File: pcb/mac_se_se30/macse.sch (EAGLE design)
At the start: 8 parts, among them J1 ATX24RH

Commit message: mac SE adaptor done
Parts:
- JP1: device pinhead:PINHD-1X3 -> atx_power_control:PINHD-1X4
- JP4: device atx_power_control:PINHD-1X4 -> adafruit_changed:PINHD-1X6
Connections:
- removed net N$7: JP1.2, JP4.3
- net +12V: now also JP1.3; no longer JP1.1
- net +5V: now also JP4.3; no longer JP1.3
- net GND: now also JP1.4
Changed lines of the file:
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@@
 </classes>
 <parts>
-<part name="GND1" library="supply1" library_urn="urn:adsk.eagle:library:371" deviceset="GND" device=""/>
 <part name="J1" library="atx4vc" deviceset="ATX24" device="RH"/>
 <part name="GND2" library="supply1" library_urn="urn:adsk.eagle:library:371" deviceset="GND" device=""/>
@@
 <part name="P-1" library="supply1" library_urn="urn:adsk.eagle:library:371" deviceset="-12V" device=""/>
 <part name="J7" library="atx_power_control" deviceset="CONN_02" device="3.5MM-NO_SILK"/>
-<part name="JP4" library="atx_power_control" deviceset="PINHD-1X4" device=""/>
+<part name="JP4" library="adafruit_changed" deviceset="PINHD-1X6" device=""/>
 <part name="U$8" library="atx_power_control" deviceset="CAR_FUSE_HOLDER" device="3IN1"/>
 <part name="U$2" library="atx_power_control" deviceset="CAR_FUSE_HOLDER" device="3IN1"/>
-<part name="JP1" library="pinhead" library_urn="urn:adsk.eagle:library:325" deviceset="PINHD-1X3" device="" package3d_urn="urn:adsk.eagle:package:22458/2"/>
 <part name="JP2" library="pinhead" library_urn="urn:adsk.eagle:library:325" deviceset="PINHD-1X2" device="" package3d_urn="urn:adsk.eagle:package:22435/2"/>
 <part name="P+3" library="supply1" library_urn="urn:adsk.eagle:library:371" deviceset="+5V" device=""/>
 <part name="P+1" library="supply1" library_urn="urn:adsk.eagle:library:371" deviceset="+12V" device=""/>
 <part name="P-2" library="supply1" library_urn="urn:adsk.eagle:library:371" deviceset="-12V" device=""/>
-<part name="P+4" library="supply1" library_urn="urn:adsk.eagle:library:371" deviceset="+5V" device=""/>
 <part name="GND3" library="supply1" library_urn="urn:adsk.eagle:library:371" deviceset="GND" device=""/>
 <part name="GND4" library="supply1" library_urn="urn:adsk.eagle:library:371" deviceset="GND" device=""/>
 <part name="P+5" library="supply1" library_urn="urn:adsk.eagle:library:371" deviceset="+12V" device=""/>
-<part name="P+6" library="supply1" library_urn="urn:adsk.eagle:library:371" deviceset="+5V" device=""/>
-<part name="GND5" library="supply1" library_urn="urn:adsk.eagle:library:371" deviceset="GND" device=""/>
 <part name="U$1" library="atx4vc" deviceset="MACSE" device=""/>
 <part name="GND6" library="supply1" library_urn="urn:adsk.eagle:library:371" deviceset="GND" device=""/>
 <part name="P+7" library="supply1" library_urn="urn:adsk.eagle:library:371" deviceset="+5V" device=""/>
+<part name="JP1" library="atx_power_control" deviceset="PINHD-1X4" device=""/>
+<part name="GND7" library="supply1" library_urn="urn:adsk.eagle:library:371" deviceset="GND" device=""/>
+<part name="P+9" library="supply1" library_urn="urn:adsk.eagle:library:371" deviceset="+5V" device=""/>
 </parts>
 <sheets>
@@
 </plain>
 <instances>
-<instance part="GND1" gate="1" x="157.48" y="88.9" smashed="yes">
-<attribute name="VALUE" x="154.94" y="86.36" size="1.778" layer="96"/>
-</instance>
 <instance part="J1" gate="G$1" x="96.52" y="175.26" smashed="yes">
 <attribute name="NAME" x="83.82" y="195.58" size="1.27" layer="95"/>
@@
 <attribute name="NAME" x="167.64" y="156.972" size="1.778" layer="95" font="vector" rot="R180"/>
 </instance>
-<instance part="JP4" gate="A" x="-15.24" y="101.6" smashed="yes">
-<attribute name="NAME" x="-21.59" y="109.855" size="1.778" layer="95"/>
-<attribute name="VALUE" x="-21.59" y="93.98" size="1.778" layer="96"/>
+<instance part="JP4" gate="A" x="-15.24" y="99.06" smashed="yes">
+<attribute name="NAME" x="-21.59" y="107.315" size="1.778" layer="95"/>
+<attribute name="VALUE" x="-21.59" y="91.44" size="1.778" layer="96"/>
 </instance>
 <instance part="U$8" gate="G$1" x="38.1" y="187.96" smashed="yes"/>
 <instance part="U$2" gate="G$1" x="154.94" y="175.26" smashed="yes"/>
-<instance part="JP1" gate="A" x="5.08" y="101.6" smashed="yes">
-<attribute name="NAME" x="-1.27" y="107.315" size="1.778" layer="95"/>
-<attribute name="VALUE" x="-1.27" y="93.98" size="1.778" layer="96"/>
-</instance>
 <instance part="JP2" gate="G$1" x="180.34" y="160.02" smashed="yes">
 <attribute name="NAME" x="173.99" y="165.735" size="1.778" layer="95"/>
@@
 <attribute name="VALUE" x="114.3" y="101.6" size="1.778" layer="96" rot="MR90"/>
 </instance>
-<instance part="P+4" gate="1" x="149.86" y="109.22" smashed="yes">
-<attribute name="VALUE" x="147.32" y="104.14" size="1.778" layer="96" rot="R90"/>
-</instance>
 <instance part="GND3" gate="1" x="149.86" y="157.48" smashed="yes">
 <attribute name="VALUE" x="147.32" y="154.94" size="1.778" layer="96"/>
@@
 <attribute name="VALUE" x="-30.48" y="93.98" size="1.778" layer="96"/>
 </instance>
-<instance part="P+5" gate="1" x="15.24" y="106.68" smashed="yes" rot="MR0">
-<attribute name="VALUE" x="17.78" y="101.6" size="1.778" layer="96" rot="MR90"/>
-</instance>
-<instance part="P+6" gate="1" x="25.4" y="101.6" smashed="yes">
-<attribute name="VALUE" x="22.86" y="96.52" size="1.778" layer="96" rot="R90"/>
-</instance>
-<instance part="GND5" gate="1" x="177.8" y="73.66" smashed="yes">
-<attribute name="VALUE" x="175.26" y="71.12" size="1.778" layer="96"/>
+<instance part="P+5" gate="1" x="-7.62" y="137.16" smashed="yes" rot="MR0">
+<attribute name="VALUE" x="-5.08" y="132.08" size="1.778" layer="96" rot="MR90"/>
 </instance>
 <instance part="U$1" gate="G$1" x="83.82" y="109.22" smashed="yes"/>
@@
 <instance part="P+7" gate="1" x="121.92" y="119.38" smashed="yes">
 <attribute name="VALUE" x="119.38" y="114.3" size="1.778" layer="96" rot="R90"/>
+</instance>
+<instance part="JP1" gate="A" x="-15.24" y="134.62" smashed="yes">
+<attribute name="NAME" x="-21.59" y="142.875" size="1.778" layer="95"/>
+<attribute name="VALUE" x="-21.59" y="127" size="1.778" layer="96"/>
+</instance>
+<instance part="GND7" gate="1" x="-27.94" y="129.54" smashed="yes">
+<attribute name="VALUE" x="-30.48" y="127" size="1.778" layer="96"/>
+</instance>
+<instance part="P+9" gate="1" x="-5.08" y="104.14" smashed="yes">
+<attribute name="VALUE" x="-7.62" y="99.06" size="1.778" layer="96" rot="R90"/>
 </instance>
 </instances>
@@
 <junction x="106.68" y="96.52"/>
 </segment>
+<segment>
+<pinref part="JP1" gate="A" pin="4"/>
+<pinref part="GND7" gate="1" pin="GND"/>
+<wire x1="-17.78" y1="132.08" x2="-27.94" y2="132.08" width="0.1524" layer="91"/>
+</segment>
 </net>
 <net name="-12V" class="0">
@@
 </segment>
 <segment>
-<pinref part="JP1" gate="A" pin="3"/>
-<pinref part="P+6" gate="1" pin="+5V"/>
-<wire x1="2.54" y1="99.06" x2="25.4" y2="99.06" width="0.1524" layer="91"/>
-</segment>
-<segment>
 <pinref part="U$1" gate="G$1" pin="P$4"/>
 <pinref part="P+7" gate="1" pin="+5V"/>
@@
 <wire x1="121.92" y1="91.44" x2="73.66" y2="91.44" width="0.1524" layer="91"/>
 <junction x="121.92" y="116.84"/>
+</segment>
+<segment>
+<pinref part="JP4" gate="A" pin="3"/>
+<pinref part="P+9" gate="1" pin="+5V"/>
+<wire x1="-17.78" y1="101.6" x2="-5.08" y2="101.6" width="0.1524" layer="91"/>
 </segment>
 </net>
@@
 </segment>
 <segment>
-<pinref part="P+5" gate="1" pin="+12V"/>
-<pinref part="JP1" gate="A" pin="1"/>
-<wire x1="15.24" y1="104.14" x2="2.54" y2="104.14" width="0.1524" layer="91"/>
-</segment>
-<segment>
 <pinref part="U$1" gate="G$1" pin="P$5"/>
 <pinref part="P+1" gate="1" pin="+12V"/>
@@
 <junction x="53.34" y="111.76"/>
 </segment>
+<segment>
+<pinref part="JP1" gate="A" pin="3"/>
+<pinref part="P+5" gate="1" pin="+12V"/>
+<wire x1="-17.78" y1="134.62" x2="-7.62" y2="134.62" width="0.1524" layer="91"/>
+</segment>
 </net>
 <net name="N$5" class="0">
@@
 </segment>
 </net>
-<net name="N$7" class="0">
-<segment>
-<pinref part="JP1" gate="A" pin="2"/>
-<pinref part="JP4" gate="A" pin="3"/>
-<wire x1="2.54" y1="101.6" x2="-17.78" y2="101.6" width="0.1524" layer="91"/>
-</segment>
-</net>

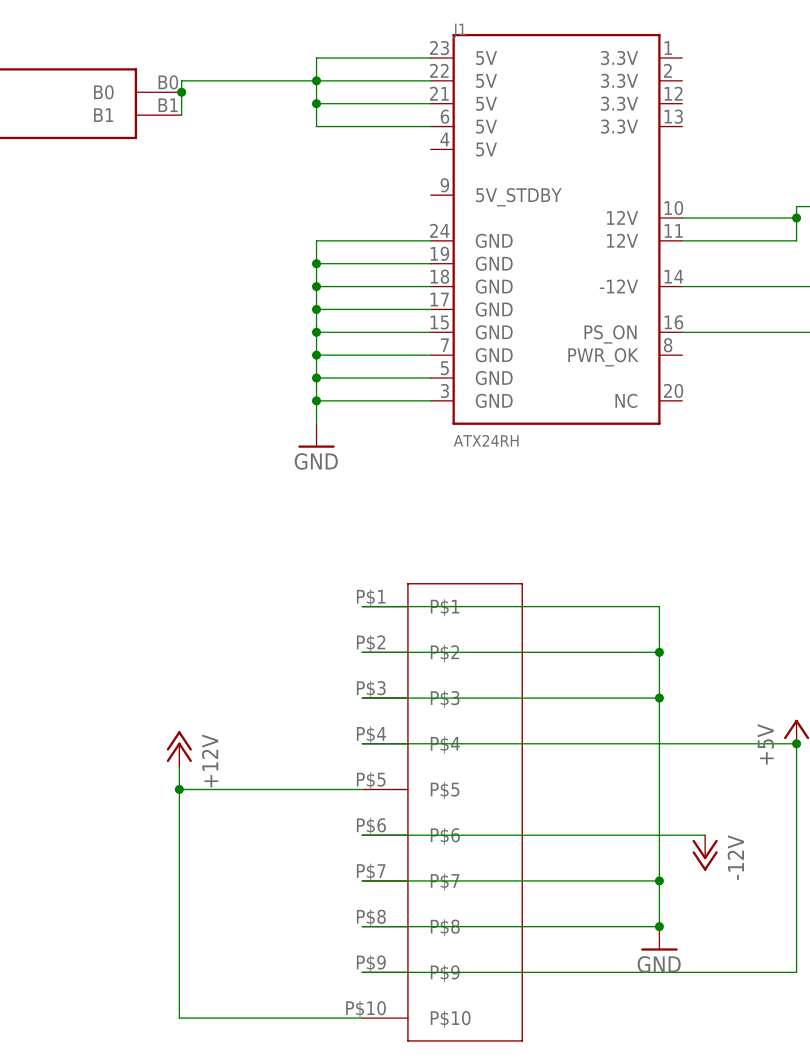
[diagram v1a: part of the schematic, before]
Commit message: updating mac SE atx adaptor
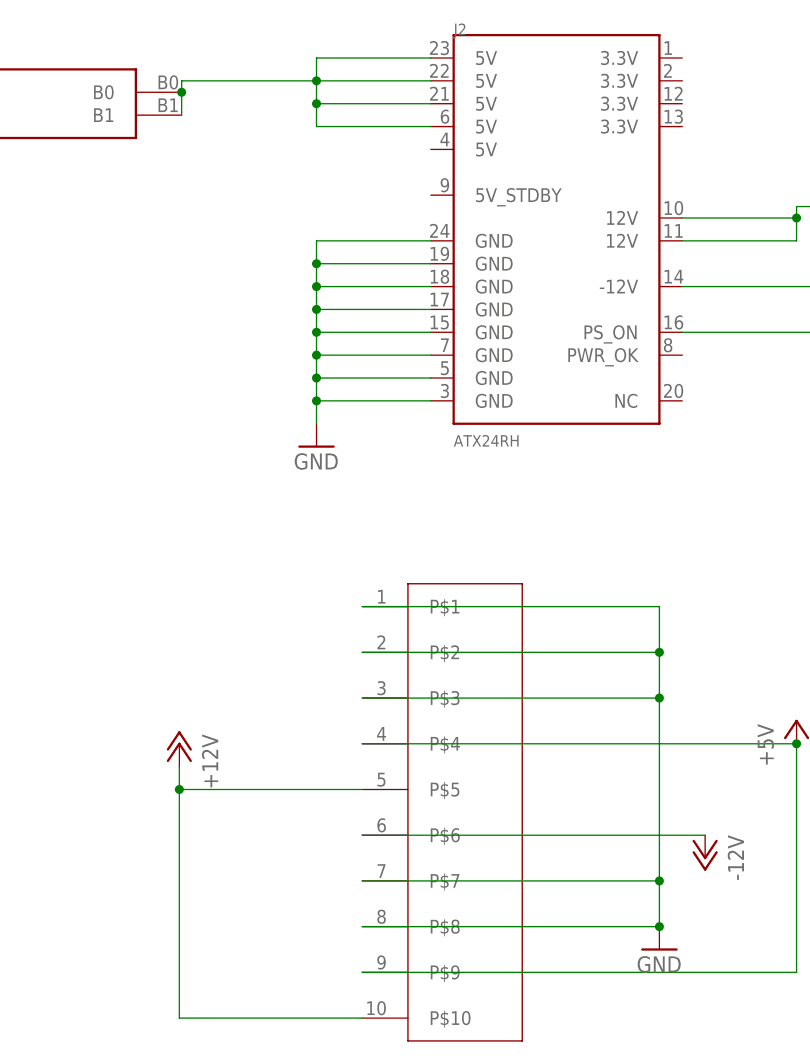
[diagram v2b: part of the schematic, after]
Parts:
- removed J1: ATX24RH, atx4vc:ATX24RH
- added J2: ATX24RH, SparkFun-Connectors:ATX24RH
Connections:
- net -12V: now also J2.-12V; no longer J1.-12V
- net GND: now also J2.GND@0, J2.GND@1, J2.GND@2, J2.GND@3, J2.GND@4, J2.GND@5, J2.GND@6, J2.GND@7; no longer J1.GND@0, J1.GND@1, J1.GND@2, J1.GND@3, J1.GND@4, J1.GND@5, J1.GND@6, J1.GND@7
- net N$5: now also J2.PS_ON; no longer J1.PS_ON
- net N$6: now also J2.5V@1, J2.5V@2, J2.5V@3, J2.5V@4; no longer J1.5V@1, J1.5V@2, J1.5V@3, J1.5V@4
- net N$8: now also J2.12V@0, J2.12V@1; no longer J1.12V@0, J1.12V@1
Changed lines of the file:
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@@
 </classes>
 <parts>
-<part name="J1" library="atx4vc" deviceset="ATX24" device="RH"/>
 <part name="GND2" library="supply1" library_urn="urn:adsk.eagle:library:371" deviceset="GND" device=""/>
 <part name="P+2" library="supply1" library_urn="urn:adsk.eagle:library:371" deviceset="+12V" device=""/>
@@
 <part name="GND7" library="supply1" library_urn="urn:adsk.eagle:library:371" deviceset="GND" device=""/>
 <part name="P+9" library="supply1" library_urn="urn:adsk.eagle:library:371" deviceset="+5V" device=""/>
+<part name="J2" library="SparkFun-Connectors" deviceset="ATX24" device="RH"/>
 </parts>
 <sheets>
@@
 </plain>
 <instances>
-<instance part="J1" gate="G$1" x="96.52" y="175.26" smashed="yes">
-<attribute name="NAME" x="83.82" y="195.58" size="1.27" layer="95"/>
-<attribute name="VALUE" x="83.82" y="149.86" size="1.27" layer="96"/>
-</instance>
 <instance part="GND2" gate="1" x="68.58" y="149.86" smashed="yes">
 <attribute name="VALUE" x="66.04" y="147.32" size="1.778" layer="96"/>
@@
 <attribute name="VALUE" x="-7.62" y="99.06" size="1.778" layer="96" rot="R90"/>
 </instance>
+<instance part="J2" gate="G$1" x="96.52" y="175.26" smashed="yes">
+<attribute name="NAME" x="83.82" y="195.58" size="1.27" layer="95"/>
+<attribute name="VALUE" x="83.82" y="149.86" size="1.27" layer="96"/>
+</instance>
 </instances>
 <busses>
@@
 <net name="GND" class="0">
 <segment>
-<pinref part="J1" gate="G$1" pin="GND@7"/>
 <pinref part="GND2" gate="1" pin="GND"/>
 <wire x1="81.28" y1="172.72" x2="68.58" y2="172.72" width="0.1524" layer="91"/>
 <wire x1="68.58" y1="172.72" x2="68.58" y2="170.18" width="0.1524" layer="91"/>
-<pinref part="J1" gate="G$1" pin="GND@6"/>
 <wire x1="68.58" y1="170.18" x2="68.58" y2="167.64" width="0.1524" layer="91"/>
 <wire x1="68.58" y1="167.64" x2="68.58" y2="165.1" width="0.1524" layer="91"/>
@@
 <wire x1="81.28" y1="170.18" x2="68.58" y2="170.18" width="0.1524" layer="91"/>
 <junction x="68.58" y="170.18"/>
-<pinref part="J1" gate="G$1" pin="GND@5"/>
 <wire x1="68.58" y1="167.64" x2="81.28" y2="167.64" width="0.1524" layer="91"/>
 <junction x="68.58" y="167.64"/>
-<pinref part="J1" gate="G$1" pin="GND@4"/>
 <wire x1="81.28" y1="165.1" x2="68.58" y2="165.1" width="0.1524" layer="91"/>
 <junction x="68.58" y="165.1"/>
-<pinref part="J1" gate="G$1" pin="GND@3"/>
 <wire x1="68.58" y1="162.56" x2="81.28" y2="162.56" width="0.1524" layer="91"/>
 <junction x="68.58" y="162.56"/>
-<pinref part="J1" gate="G$1" pin="GND@2"/>
 <wire x1="81.28" y1="160.02" x2="68.58" y2="160.02" width="0.1524" layer="91"/>
 <junction x="68.58" y="160.02"/>
-<pinref part="J1" gate="G$1" pin="GND@1"/>
 <wire x1="68.58" y1="157.48" x2="81.28" y2="157.48" width="0.1524" layer="91"/>
 <junction x="68.58" y="157.48"/>
-<pinref part="J1" gate="G$1" pin="GND@0"/>
 <wire x1="81.28" y1="154.94" x2="68.58" y2="154.94" width="0.1524" layer="91"/>
 <junction x="68.58" y="154.94"/>
+<pinref part="J2" gate="G$1" pin="GND@0"/>
+<pinref part="J2" gate="G$1" pin="GND@1"/>
+<pinref part="J2" gate="G$1" pin="GND@2"/>
+<pinref part="J2" gate="G$1" pin="GND@3"/>
+<pinref part="J2" gate="G$1" pin="GND@4"/>
+<pinref part="J2" gate="G$1" pin="GND@5"/>
+<pinref part="J2" gate="G$1" pin="GND@6"/>
+<pinref part="J2" gate="G$1" pin="GND@7"/>
 </segment>
 <segment>
@@
 <segment>
 <pinref part="P-1" gate="1" pin="-12V"/>
-<pinref part="J1" gate="G$1" pin="-12V"/>
 <wire x1="137.16" y1="167.64" x2="109.22" y2="167.64" width="0.1524" layer="91"/>
+<pinref part="J2" gate="G$1" pin="-12V"/>
 </segment>
 <segment>
@@
 <net name="N$6" class="0">
 <segment>
-<pinref part="J1" gate="G$1" pin="5V@4"/>
 <wire x1="81.28" y1="193.04" x2="68.58" y2="193.04" width="0.1524" layer="91"/>
-<pinref part="J1" gate="G$1" pin="5V@3"/>
 <wire x1="81.28" y1="190.5" x2="68.58" y2="190.5" width="0.1524" layer="91"/>
 <wire x1="68.58" y1="190.5" x2="68.58" y2="193.04" width="0.1524" layer="91"/>
-<pinref part="J1" gate="G$1" pin="5V@2"/>
 <wire x1="81.28" y1="187.96" x2="68.58" y2="187.96" width="0.1524" layer="91"/>
 <wire x1="68.58" y1="187.96" x2="68.58" y2="190.5" width="0.1524" layer="91"/>
 <junction x="68.58" y="190.5"/>
-<pinref part="J1" gate="G$1" pin="5V@1"/>
 <wire x1="81.28" y1="185.42" x2="68.58" y2="185.42" width="0.1524" layer="91"/>
 <wire x1="68.58" y1="185.42" x2="68.58" y2="187.96" width="0.1524" layer="91"/>
@@
 <wire x1="53.594" y1="190.5" x2="53.594" y2="189.23" width="0.1524" layer="91"/>
 <junction x="53.594" y="189.23"/>
+<pinref part="J2" gate="G$1" pin="5V@1"/>
+<pinref part="J2" gate="G$1" pin="5V@2"/>
+<pinref part="J2" gate="G$1" pin="5V@3"/>
+<pinref part="J2" gate="G$1" pin="5V@4"/>
 </segment>
 </net>
@@
 <net name="N$8" class="0">
 <segment>
-<pinref part="J1" gate="G$1" pin="12V@1"/>
 <wire x1="109.22" y1="172.72" x2="121.92" y2="172.72" width="0.1524" layer="91"/>
-<pinref part="J1" gate="G$1" pin="12V@0"/>
 <wire x1="109.22" y1="175.26" x2="121.92" y2="175.26" width="0.1524" layer="91"/>
 <wire x1="121.92" y1="175.26" x2="121.92" y2="172.72" width="0.1524" layer="91"/>
@@
 <wire x1="139.954" y1="173.99" x2="139.954" y2="176.53" width="0.1524" layer="91"/>
 <junction x="139.954" y="176.53"/>
+<pinref part="J2" gate="G$1" pin="12V@0"/>
+<pinref part="J2" gate="G$1" pin="12V@1"/>
 </segment>
 </net>
@@
 <net name="N$5" class="0">
 <segment>
-<pinref part="J1" gate="G$1" pin="PS_ON"/>
 <wire x1="109.22" y1="162.56" x2="157.48" y2="162.56" width="0.1524" layer="91"/>
 <pinref part="J7" gate="G$1" pin="1"/>
@@
 <wire x1="177.8" y1="162.56" x2="157.48" y2="162.56" width="0.1524" layer="91"/>
 <junction x="157.48" y="162.56"/>
-</segment>
-</net>
+<pinref part="J2" gate="G$1" pin="PS_ON"/>
+</segment>
+</net>

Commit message: updated mac SE pcb
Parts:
- removed JP4: (no value), adafruit_changed:PINHD-1X6
- added JP3: (no value), atx_power_control:PINHD-1X4
- added TP1: PTR1PAD1-20Y, testpad:PTR1PAD1-20Y
- J2: device SparkFun-Connectors:ATX24RH -> macse:ATX24RH
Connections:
- net +5V: now also JP3.3; no longer JP4.3
- net GND: now also JP3.4, TP1.TP; no longer JP4.4
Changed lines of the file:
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@@
 <part name="P-1" library="supply1" library_urn="urn:adsk.eagle:library:371" deviceset="-12V" device=""/>
 <part name="J7" library="atx_power_control" deviceset="CONN_02" device="3.5MM-NO_SILK"/>
-<part name="JP4" library="adafruit_changed" deviceset="PINHD-1X6" device=""/>
 <part name="U$8" library="atx_power_control" deviceset="CAR_FUSE_HOLDER" device="3IN1"/>
 <part name="U$2" library="atx_power_control" deviceset="CAR_FUSE_HOLDER" device="3IN1"/>
@@
 <part name="GND7" library="supply1" library_urn="urn:adsk.eagle:library:371" deviceset="GND" device=""/>
 <part name="P+9" library="supply1" library_urn="urn:adsk.eagle:library:371" deviceset="+5V" device=""/>
-<part name="J2" library="SparkFun-Connectors" deviceset="ATX24" device="RH"/>
+<part name="J2" library="macse" deviceset="ATX24" device="RH"/>
+<part name="JP3" library="atx_power_control" deviceset="PINHD-1X4" device=""/>
+<part name="TP1" library="testpad" library_urn="urn:adsk.eagle:library:385" deviceset="PTR1" device="PAD1-20Y" package3d_urn="urn:adsk.eagle:package:27951/1"/>
+<part name="GND1" library="supply1" library_urn="urn:adsk.eagle:library:371" deviceset="GND" device=""/>
 </parts>
 <sheets>
@@
 <attribute name="NAME" x="167.64" y="156.972" size="1.778" layer="95" font="vector" rot="R180"/>
 </instance>
-<instance part="JP4" gate="A" x="-15.24" y="99.06" smashed="yes">
-<attribute name="NAME" x="-21.59" y="107.315" size="1.778" layer="95"/>
-<attribute name="VALUE" x="-21.59" y="91.44" size="1.778" layer="96"/>
-</instance>
 <instance part="U$8" gate="G$1" x="38.1" y="187.96" smashed="yes"/>
 <instance part="U$2" gate="G$1" x="154.94" y="175.26" smashed="yes"/>
@@
 <attribute name="VALUE" x="147.32" y="154.94" size="1.778" layer="96"/>
 </instance>
-<instance part="GND4" gate="1" x="-27.94" y="96.52" smashed="yes">
-<attribute name="VALUE" x="-30.48" y="93.98" size="1.778" layer="96"/>
+<instance part="GND4" gate="1" x="-27.94" y="93.98" smashed="yes">
+<attribute name="VALUE" x="-30.48" y="91.44" size="1.778" layer="96"/>
 </instance>
 <instance part="P+5" gate="1" x="-7.62" y="137.16" smashed="yes" rot="MR0">
@@
 <attribute name="VALUE" x="-30.48" y="127" size="1.778" layer="96"/>
 </instance>
-<instance part="P+9" gate="1" x="-5.08" y="104.14" smashed="yes">
-<attribute name="VALUE" x="-7.62" y="99.06" size="1.778" layer="96" rot="R90"/>
+<instance part="P+9" gate="1" x="-5.08" y="101.6" smashed="yes">
+<attribute name="VALUE" x="-7.62" y="96.52" size="1.778" layer="96" rot="R90"/>
 </instance>
 <instance part="J2" gate="G$1" x="96.52" y="175.26" smashed="yes">
 <attribute name="NAME" x="83.82" y="195.58" size="1.27" layer="95"/>
 <attribute name="VALUE" x="83.82" y="149.86" size="1.27" layer="96"/>
+</instance>
+<instance part="JP3" gate="A" x="-15.24" y="99.06" smashed="yes">
+<attribute name="NAME" x="-21.59" y="107.315" size="1.778" layer="95"/>
+<attribute name="VALUE" x="-21.59" y="91.44" size="1.778" layer="96"/>
+</instance>
+<instance part="TP1" gate="G$1" x="137.16" y="142.24" smashed="yes">
+<attribute name="NAME" x="136.144" y="135.89" size="1.778" layer="95" rot="R90"/>
+<attribute name="TP_SIGNAL_NAME" x="138.43" y="139.7" size="1.778" layer="97"/>
+</instance>
+<instance part="GND1" gate="1" x="144.78" y="142.24" smashed="yes">
+<attribute name="VALUE" x="142.24" y="139.7" size="1.778" layer="96"/>
 </instance>
 </instances>
@@
 </segment>
 <segment>
-<pinref part="JP4" gate="A" pin="4"/>
 <pinref part="GND4" gate="1" pin="GND"/>
-<wire x1="-17.78" y1="99.06" x2="-27.94" y2="99.06" width="0.1524" layer="91"/>
+<wire x1="-17.78" y1="96.52" x2="-27.94" y2="96.52" width="0.1524" layer="91"/>
+<pinref part="JP3" gate="A" pin="4"/>
 </segment>
 <segment>
@@
 <wire x1="-17.78" y1="132.08" x2="-27.94" y2="132.08" width="0.1524" layer="91"/>
 </segment>
+<segment>
+<pinref part="TP1" gate="G$1" pin="TP"/>
+<pinref part="GND1" gate="1" pin="GND"/>
+<wire x1="137.16" y1="144.78" x2="144.78" y2="144.78" width="0.1524" layer="91"/>
+</segment>
 </net>
 <net name="-12V" class="0">
@@
 </segment>
 <segment>
-<pinref part="JP4" gate="A" pin="3"/>
 <pinref part="P+9" gate="1" pin="+5V"/>
-<wire x1="-17.78" y1="101.6" x2="-5.08" y2="101.6" width="0.1524" layer="91"/>
-</segment>
-</net>
+<wire x1="-17.78" y1="99.06" x2="-5.08" y2="99.06" width="0.1524" layer="91"/>
+<pinref part="JP3" gate="A" pin="3"/>
+</segment>
+</net>
